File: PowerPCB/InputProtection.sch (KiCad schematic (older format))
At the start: 5 parts

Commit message: Added footprints for resistors and capacitors
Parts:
- C9: footprint (none) -> Capacitor_SMD:C_0805_2012Metric_Pad1.15x1.40mm_HandSolder
- D6, D7: footprint SOD3716X145N -> SamacSys_Parts:SOD3716X145N
- R17, R18: footprint (none) -> Resistor_SMD:R_0805_2012Metric_Pad1.15x1.40mm_HandSolder
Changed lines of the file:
@@
 $Descr A4 11693 8268
 encoding utf-8
-Sheet 4 5
+Sheet 5 5
 Title ""
 Date ""
@@
 F 0 "R21" V 1193 1850 50  0000 C CNN
 F 1 "10" V 1284 1850 50  0000 C CNN
-F 2 "" V 1330 1850 50  0001 C CNN
+F 2 "Resistor_SMD:R_0805_2012Metric_Pad1.15x1.40mm_HandSolder" V 1330 1850 50  0001 C CNN
 F 3 "~" H 1400 1850 50  0001 C CNN
 	1    1400 1850
@@
 F 0 "C11" H 2665 2296 50  0000 L CNN
 F 1 "10u" H 2665 2205 50  0000 L CNN
-F 2 "" H 2588 2100 50  0001 C CNN
+F 2 "Capacitor_SMD:C_0805_2012Metric_Pad1.15x1.40mm_HandSolder" H 2588 2100 50  0001 C CNN
 F 3 "~" H 2550 2250 50  0001 C CNN
 	1    2550 2250
@@
 F 0 "R22" V 1943 1850 50  0000 C CNN
 F 1 "1k" V 2034 1850 50  0000 C CNN
-F 2 "" V 2080 1850 50  0001 C CNN
+F 2 "Resistor_SMD:R_0805_2012Metric_Pad1.15x1.40mm_HandSolder" V 2080 1850 50  0001 C CNN
 F 3 "~" H 2150 1850 50  0001 C CNN
 	1    2150 1850
@@
 F 0 "D10" V 1904 1178 50  0000 L CNN
 F 1 "1N5819HW-7-F" V 1995 1178 50  0000 L CNN
-F 2 "SOD3716X145N" H 2100 1050 50  0001 L CNN
+F 2 "SamacSys_Parts:SOD3716X145N" H 2100 1050 50  0001 L CNN
 F 3 "http://www.diodes.com/_files/datasheets/ds30217.pdf" H 2100 950 50  0001 L CNN
 F 4 "Diode Schottky 1A 40V SOD123 Diodes Inc 1N5819HW-7-F, SMT Schottky Diode, 40V 1A, 2-Pin SOD-123" H 2100 850 50  0001 L CNN "Description"
@@
 F 0 "D11" V 1904 2078 50  0000 L CNN
 F 1 "1N5819HW-7-F" V 1995 2078 50  0000 L CNN
-F 2 "SOD3716X145N" H 2100 1950 50  0001 L CNN
+F 2 "SamacSys_Parts:SOD3716X145N" H 2100 1950 50  0001 L CNN
 F 3 "http://www.diodes.com/_files/datasheets/ds30217.pdf" H 2100 1850 50  0001 L CNN
 F 4 "Diode Schottky 1A 40V SOD123 Diodes Inc 1N5819HW-7-F, SMT Schottky Diode, 40V 1A, 2-Pin SOD-123" H 2100 1750 50  0001 L CNN "Description"

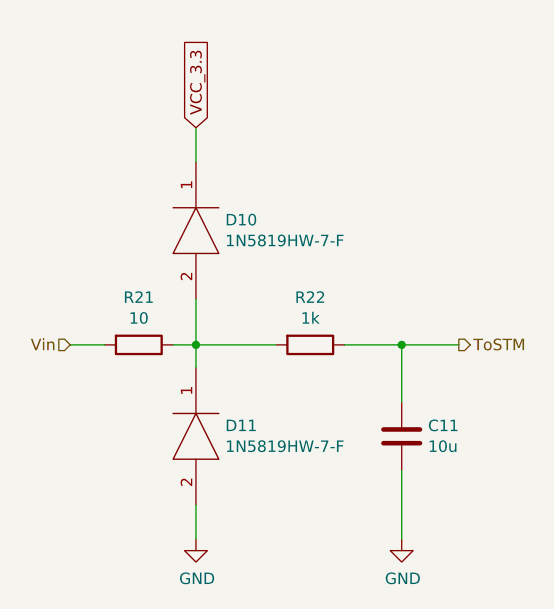
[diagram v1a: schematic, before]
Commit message: Changed Shottky diodes to 0805 size
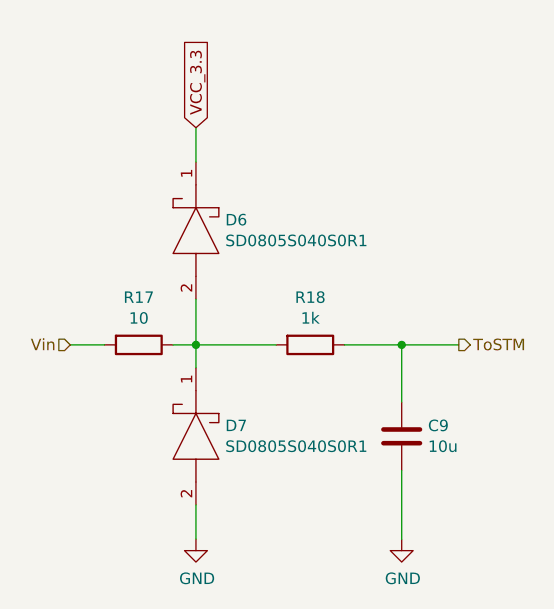
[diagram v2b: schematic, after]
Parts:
- removed D6, D7: 1N5819HW-7-F, SamacSys_Parts:SOD3716X145N, symbol SamacSys_Parts:1N5819HW-7-F
- added D8, D9: SD0805S040S0R1, SamacSys_Parts:DIOM2013X100N, symbol SamacSys_Parts:SD0805S040S0R1
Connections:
- net GND: now also D9.2
- net VCC_3.3: now also D8.1
- net at R17.1, R18.2: now also D8.2, D9.1
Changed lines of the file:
@@
 $Descr A4 11693 8268
 encoding utf-8
-Sheet 5 5
+Sheet 3 5
 Title ""
 Date ""
@@
 AR Path="/5EE3728E/5EE2BE9C" Ref="R19"  Part="1"
 AR Path="/5EE40591/5EE2BE9C" Ref="R21"  Part="1"
-F 0 "R21" V 1193 1850 50  0000 C CNN
+F 0 "R17" V 1193 1850 50  0000 C CNN
 F 1 "10" V 1284 1850 50  0000 C CNN
 F 2 "Resistor_SMD:R_0805_2012Metric_Pad1.15x1.40mm_HandSolder" V 1330 1850 50  0001 C CNN
@@
 AR Path="/5EE3728E/5EE2CD90" Ref="C10"  Part="1"
 AR Path="/5EE40591/5EE2CD90" Ref="C11"  Part="1"
-F 0 "C11" H 2665 2296 50  0000 L CNN
+F 0 "C9" H 2665 2296 50  0000 L CNN
 F 1 "10u" H 2665 2205 50  0000 L CNN
 F 2 "Capacitor_SMD:C_0805_2012Metric_Pad1.15x1.40mm_HandSolder" H 2588 2100 50  0001 C CNN
@@
 AR Path="/5EE3728E/5EE2F40D" Ref="R20"  Part="1"
 AR Path="/5EE40591/5EE2F40D" Ref="R22"  Part="1"
-F 0 "R22" V 1943 1850 50  0000 C CNN
+F 0 "R18" V 1943 1850 50  0000 C CNN
 F 1 "1k" V 2034 1850 50  0000 C CNN
 F 2 "Resistor_SMD:R_0805_2012Metric_Pad1.15x1.40mm_HandSolder" V 2080 1850 50  0001 C CNN
@@
 AR Path="/5EE3728E/5EE31FD8" Ref="#PWR025"  Part="1"
 AR Path="/5EE40591/5EE31FD8" Ref="#PWR027"  Part="1"
-F 0 "#PWR027" H 1650 2450 50  0001 C CNN
+F 0 "#PWR023" H 1650 2450 50  0001 C CNN
 F 1 "GND" H 1655 2527 50  0000 C CNN
 F 2 "" H 1650 2700 50  0001 C CNN
@@
 AR Path="/5EE3728E/5EE33069" Ref="#PWR026"  Part="1"
 AR Path="/5EE40591/5EE33069" Ref="#PWR028"  Part="1"
-F 0 "#PWR028" H 2550 2450 50  0001 C CNN
+F 0 "#PWR024" H 2550 2450 50  0001 C CNN
 F 1 "GND" H 2555 2527 50  0000 C CNN
 F 2 "" H 2550 2700 50  0001 C CNN
@@
 Text HLabel 2800 1850 2    50   Output ~ 0
 ToSTM
-$Comp
-L SamacSys_Parts:1N5819HW-7-F D6
-U 1 1 5EE2FF26
-P 1650 1050
-AR Path="/5EE2B52D/5EE2FF26" Ref="D6"  Part="1"
-AR Path="/5EE3728E/5EE2FF26" Ref="D8"  Part="1"
-AR Path="/5EE40591/5EE2FF26" Ref="D10"  Part="1"
-F 0 "D10" V 1904 1178 50  0000 L CNN
-F 1 "1N5819HW-7-F" V 1995 1178 50  0000 L CNN
-F 2 "SamacSys_Parts:SOD3716X145N" H 2100 1050 50  0001 L CNN
-F 3 "http://www.diodes.com/_files/datasheets/ds30217.pdf" H 2100 950 50  0001 L CNN
-F 4 "Diode Schottky 1A 40V SOD123 Diodes Inc 1N5819HW-7-F, SMT Schottky Diode, 40V 1A, 2-Pin SOD-123" H 2100 850 50  0001 L CNN "Description"
-F 5 "1.45" H 2100 750 50  0001 L CNN "Height"
-F 6 "621-1N5819HW-F" H 2100 650 50  0001 L CNN "Mouser Part Number"
-F 7 "https://www.mouser.co.uk/ProductDetail/Diodes-Incorporated/1N5819HW-7-F?qs=NQ47qNm99eDyWTEd07miYA%3D%3D" H 2100 550 50  0001 L CNN "Mouser Price/Stock"
-F 8 "Diodes Inc." H 2100 450 50  0001 L CNN "Manufacturer_Name"
-F 9 "1N5819HW-7-F" H 2100 350 50  0001 L CNN "Manufacturer_Part_Number"
-	1    1650 1050
-	0    1    1    0
-$EndComp
-$Comp
-L SamacSys_Parts:1N5819HW-7-F D7
-U 1 1 5EE3329F
-P 1650 1950
-AR Path="/5EE2B52D/5EE3329F" Ref="D7"  Part="1"
-AR Path="/5EE3728E/5EE3329F" Ref="D9"  Part="1"
-AR Path="/5EE40591/5EE3329F" Ref="D11"  Part="1"
-F 0 "D11" V 1904 2078 50  0000 L CNN
-F 1 "1N5819HW-7-F" V 1995 2078 50  0000 L CNN
-F 2 "SamacSys_Parts:SOD3716X145N" H 2100 1950 50  0001 L CNN
-F 3 "http://www.diodes.com/_files/datasheets/ds30217.pdf" H 2100 1850 50  0001 L CNN
-F 4 "Diode Schottky 1A 40V SOD123 Diodes Inc 1N5819HW-7-F, SMT Schottky Diode, 40V 1A, 2-Pin SOD-123" H 2100 1750 50  0001 L CNN "Description"
-F 5 "1.45" H 2100 1650 50  0001 L CNN "Height"
-F 6 "621-1N5819HW-F" H 2100 1550 50  0001 L CNN "Mouser Part Number"
-F 7 "https://www.mouser.co.uk/ProductDetail/Diodes-Incorporated/1N5819HW-7-F?qs=NQ47qNm99eDyWTEd07miYA%3D%3D" H 2100 1450 50  0001 L CNN "Mouser Price/Stock"
-F 8 "Diodes Inc." H 2100 1350 50  0001 L CNN "Manufacturer_Name"
-F 9 "1N5819HW-7-F" H 2100 1250 50  0001 L CNN "Manufacturer_Part_Number"
-	1    1650 1950
-	0    1    1    0
-$EndComp
 Wire Wire Line
 	2550 2400 2550 2700
@@
 Wire Wire Line
 	2550 1850 2800 1850
+$Comp
+L SamacSys_Parts:SD0805S040S0R1 D8
+U 1 1 5EE55C00
+P 1650 950
+AR Path="/5EE3728E/5EE55C00" Ref="D8"  Part="1"
+AR Path="/5EE2B52D/5EE55C00" Ref="D6"  Part="1"
+AR Path="/5EE40591/5EE55C00" Ref="D10"  Part="1"
+F 0 "D6" V 2004 1078 50  0000 L CNN
+F 1 "SD0805S040S0R1" V 2095 1078 50  0000 L CNN
+F 2 "SamacSys_Parts:DIOM2013X100N" H 2150 1100 50  0001 L CNN
+F 3 "https://componentsearchengine.com/Datasheets/1/SD0805S040S0R1.pdf" H 2150 1000 50  0001 L CNN
+F 4 "Schottky Diodes & Rectifiers 40volts 0.1A SIZE 0805" H 2150 900 50  0001 L CNN "Description"
+F 5 "1" H 2150 800 50  0001 L CNN "Height"
+F 6 "581-SD0805S040S0R1" H 2150 700 50  0001 L CNN "Mouser Part Number"
+F 7 "https://www.mouser.co.uk/ProductDetail/AVX/SD0805S040S0R1?qs=jCA%252BPfw4LHYgtNhiwPuw4Q%3D%3D" H 2150 600 50  0001 L CNN "Mouser Price/Stock"
+F 8 "AVX" H 2150 500 50  0001 L CNN "Manufacturer_Name"
+F 9 "SD0805S040S0R1" H 2150 400 50  0001 L CNN "Manufacturer_Part_Number"
+	1    1650 950
+	0    1    1    0
+$EndComp
+$Comp
+L SamacSys_Parts:SD0805S040S0R1 D9
+U 1 1 5EE57F4B
+P 1650 1850
+AR Path="/5EE3728E/5EE57F4B" Ref="D9"  Part="1"
+AR Path="/5EE2B52D/5EE57F4B" Ref="D7"  Part="1"
+AR Path="/5EE40591/5EE57F4B" Ref="D11"  Part="1"
+F 0 "D7" V 2004 1978 50  0000 L CNN
+F 1 "SD0805S040S0R1" V 2095 1978 50  0000 L CNN
+F 2 "SamacSys_Parts:DIOM2013X100N" H 2150 2000 50  0001 L CNN
+F 3 "https://componentsearchengine.com/Datasheets/1/SD0805S040S0R1.pdf" H 2150 1900 50  0001 L CNN
+F 4 "Schottky Diodes & Rectifiers 40volts 0.1A SIZE 0805" H 2150 1800 50  0001 L CNN "Description"
+F 5 "1" H 2150 1700 50  0001 L CNN "Height"
+F 6 "581-SD0805S040S0R1" H 2150 1600 50  0001 L CNN "Mouser Part Number"
+F 7 "https://www.mouser.co.uk/ProductDetail/AVX/SD0805S040S0R1?qs=jCA%252BPfw4LHYgtNhiwPuw4Q%3D%3D" H 2150 1500 50  0001 L CNN "Mouser Price/Stock"
+F 8 "AVX" H 2150 1400 50  0001 L CNN "Manufacturer_Name"
+F 9 "SD0805S040S0R1" H 2150 1300 50  0001 L CNN "Manufacturer_Part_Number"
+	1    1650 1850
+	0    1    1    0
+$EndComp
 $EndSCHEMATC

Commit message: Added bypass capacitors to CAN transceivers
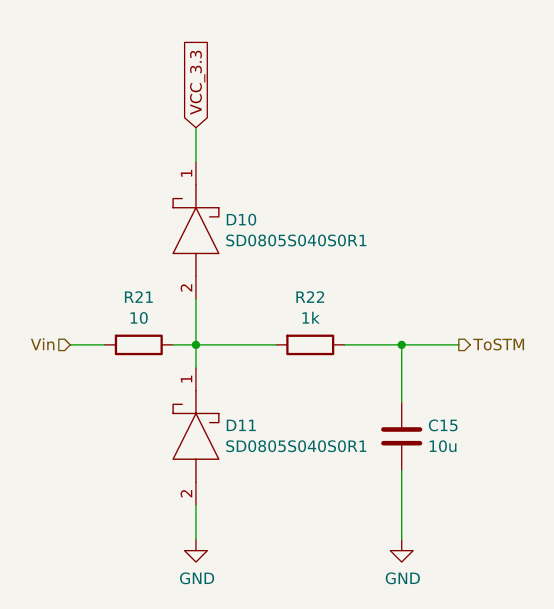
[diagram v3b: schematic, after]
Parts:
- renumbered C9 to C13
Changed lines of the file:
@@
 AR Path="/5EE3728E/5EE2BE9C" Ref="R19"  Part="1"
 AR Path="/5EE40591/5EE2BE9C" Ref="R21"  Part="1"
-F 0 "R17" V 1193 1850 50  0000 C CNN
+F 0 "R21" V 1193 1850 50  0000 C CNN
 F 1 "10" V 1284 1850 50  0000 C CNN
 F 2 "Resistor_SMD:R_0805_2012Metric_Pad1.15x1.40mm_HandSolder" V 1330 1850 50  0001 C CNN
@@
 $EndComp
 $Comp
-L Device:C C9
+L Device:C C13
 U 1 1 5EE2CD90
 P 2550 2250
-AR Path="/5EE2B52D/5EE2CD90" Ref="C9"  Part="1"
-AR Path="/5EE3728E/5EE2CD90" Ref="C10"  Part="1"
-AR Path="/5EE40591/5EE2CD90" Ref="C11"  Part="1"
-F 0 "C9" H 2665 2296 50  0000 L CNN
+AR Path="/5EE2B52D/5EE2CD90" Ref="C13"  Part="1"
+AR Path="/5EE3728E/5EE2CD90" Ref="C14"  Part="1"
+AR Path="/5EE40591/5EE2CD90" Ref="C15"  Part="1"
+F 0 "C15" H 2665 2296 50  0000 L CNN
 F 1 "10u" H 2665 2205 50  0000 L CNN
 F 2 "Capacitor_SMD:C_0805_2012Metric_Pad1.15x1.40mm_HandSolder" H 2588 2100 50  0001 C CNN
@@
 AR Path="/5EE3728E/5EE2F40D" Ref="R20"  Part="1"
 AR Path="/5EE40591/5EE2F40D" Ref="R22"  Part="1"
-F 0 "R18" V 1943 1850 50  0000 C CNN
+F 0 "R22" V 1943 1850 50  0000 C CNN
 F 1 "1k" V 2034 1850 50  0000 C CNN
 F 2 "Resistor_SMD:R_0805_2012Metric_Pad1.15x1.40mm_HandSolder" V 2080 1850 50  0001 C CNN
@@
 	1650 1950 1650 1850
 $Comp
-L power:GND #PWR023
+L power:GND #PWR028
 U 1 1 5EE31FD8
 P 1650 2700
-AR Path="/5EE2B52D/5EE31FD8" Ref="#PWR023"  Part="1"
-AR Path="/5EE3728E/5EE31FD8" Ref="#PWR025"  Part="1"
-AR Path="/5EE40591/5EE31FD8" Ref="#PWR027"  Part="1"
-F 0 "#PWR023" H 1650 2450 50  0001 C CNN
+AR Path="/5EE2B52D/5EE31FD8" Ref="#PWR028"  Part="1"
+AR Path="/5EE3728E/5EE31FD8" Ref="#PWR030"  Part="1"
+AR Path="/5EE40591/5EE31FD8" Ref="#PWR032"  Part="1"
+F 0 "#PWR032" H 1650 2450 50  0001 C CNN
 F 1 "GND" H 1655 2527 50  0000 C CNN
 F 2 "" H 1650 2700 50  0001 C CNN
@@
 	1650 2700 1650 2550
 $Comp
-L power:GND #PWR024
+L power:GND #PWR029
 U 1 1 5EE33069
 P 2550 2700
-AR Path="/5EE2B52D/5EE33069" Ref="#PWR024"  Part="1"
-AR Path="/5EE3728E/5EE33069" Ref="#PWR026"  Part="1"
-AR Path="/5EE40591/5EE33069" Ref="#PWR028"  Part="1"
-F 0 "#PWR024" H 2550 2450 50  0001 C CNN
+AR Path="/5EE2B52D/5EE33069" Ref="#PWR029"  Part="1"
+AR Path="/5EE3728E/5EE33069" Ref="#PWR031"  Part="1"
+AR Path="/5EE40591/5EE33069" Ref="#PWR033"  Part="1"
+F 0 "#PWR033" H 2550 2450 50  0001 C CNN
 F 1 "GND" H 2555 2527 50  0000 C CNN
 F 2 "" H 2550 2700 50  0001 C CNN
@@
 	2550 1850 2800 1850
 $Comp
+L SamacSys_Parts:SD0805S040S0R1 D9
+U 1 1 5EE57F4B
+P 1650 1850
+AR Path="/5EE3728E/5EE57F4B" Ref="D9"  Part="1"
+AR Path="/5EE2B52D/5EE57F4B" Ref="D7"  Part="1"
+AR Path="/5EE40591/5EE57F4B" Ref="D11"  Part="1"
+F 0 "D11" V 2004 1978 50  0000 L CNN
+F 1 "SD0805S040S0R1" V 2095 1978 50  0000 L CNN
+F 2 "SamacSys_Parts:DIOM2013X100N" H 2150 2000 50  0001 L CNN
+F 3 "https://componentsearchengine.com/Datasheets/1/SD0805S040S0R1.pdf" H 2150 1900 50  0001 L CNN
+F 4 "Schottky Diodes & Rectifiers 40volts 0.1A SIZE 0805" H 2150 1800 50  0001 L CNN "Description"
+F 5 "1" H 2150 1700 50  0001 L CNN "Height"
+F 6 "581-SD0805S040S0R1" H 2150 1600 50  0001 L CNN "Mouser Part Number"
+F 7 "https://www.mouser.co.uk/ProductDetail/AVX/SD0805S040S0R1?qs=jCA%252BPfw4LHYgtNhiwPuw4Q%3D%3D" H 2150 1500 50  0001 L CNN "Mouser Price/Stock"
+F 8 "AVX" H 2150 1400 50  0001 L CNN "Manufacturer_Name"
+F 9 "SD0805S040S0R1" H 2150 1300 50  0001 L CNN "Manufacturer_Part_Number"
+	1    1650 1850
+	0    1    1    0
+$EndComp
+$Comp
 L SamacSys_Parts:SD0805S040S0R1 D8
 U 1 1 5EE55C00
@@
 AR Path="/5EE2B52D/5EE55C00" Ref="D6"  Part="1"
 AR Path="/5EE40591/5EE55C00" Ref="D10"  Part="1"
-F 0 "D6" V 2004 1078 50  0000 L CNN
+F 0 "D10" V 2004 1078 50  0000 L CNN
 F 1 "SD0805S040S0R1" V 2095 1078 50  0000 L CNN
 F 2 "SamacSys_Parts:DIOM2013X100N" H 2150 1100 50  0001 L CNN
@@
 	0    1    1    0
 $EndComp
-$Comp
-L SamacSys_Parts:SD0805S040S0R1 D9
-U 1 1 5EE57F4B
-P 1650 1850
-AR Path="/5EE3728E/5EE57F4B" Ref="D9"  Part="1"
-AR Path="/5EE2B52D/5EE57F4B" Ref="D7"  Part="1"
-AR Path="/5EE40591/5EE57F4B" Ref="D11"  Part="1"
-F 0 "D7" V 2004 1978 50  0000 L CNN
-F 1 "SD0805S040S0R1" V 2095 1978 50  0000 L CNN
-F 2 "SamacSys_Parts:DIOM2013X100N" H 2150 2000 50  0001 L CNN
-F 3 "https://componentsearchengine.com/Datasheets/1/SD0805S040S0R1.pdf" H 2150 1900 50  0001 L CNN
-F 4 "Schottky Diodes & Rectifiers 40volts 0.1A SIZE 0805" H 2150 1800 50  0001 L CNN "Description"
-F 5 "1" H 2150 1700 50  0001 L CNN "Height"
-F 6 "581-SD0805S040S0R1" H 2150 1600 50  0001 L CNN "Mouser Part Number"
-F 7 "https://www.mouser.co.uk/ProductDetail/AVX/SD0805S040S0R1?qs=jCA%252BPfw4LHYgtNhiwPuw4Q%3D%3D" H 2150 1500 50  0001 L CNN "Mouser Price/Stock"
-F 8 "AVX" H 2150 1400 50  0001 L CNN "Manufacturer_Name"
-F 9 "SD0805S040S0R1" H 2150 1300 50  0001 L CNN "Manufacturer_Part_Number"
-	1    1650 1850
-	0    1    1    0
-$EndComp

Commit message: Added VDD bypass capacitors and values for all components
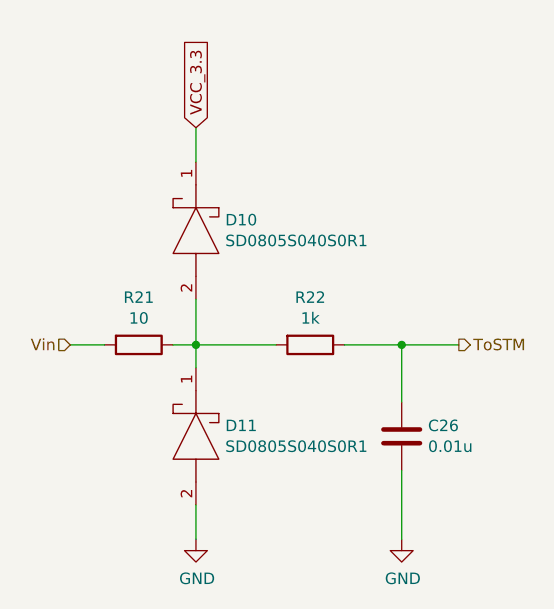
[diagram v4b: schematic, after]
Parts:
- C24: renamed from C13; value 10u -> 0.01u
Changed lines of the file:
@@
 $Descr A4 11693 8268
 encoding utf-8
-Sheet 3 5
+Sheet 5 5
 Title ""
 Date ""
@@
 $EndComp
 $Comp
-L Device:C C13
+L Device:C C24
 U 1 1 5EE2CD90
 P 2550 2250
-AR Path="/5EE2B52D/5EE2CD90" Ref="C13"  Part="1"
-AR Path="/5EE3728E/5EE2CD90" Ref="C14"  Part="1"
-AR Path="/5EE40591/5EE2CD90" Ref="C15"  Part="1"
-F 0 "C15" H 2665 2296 50  0000 L CNN
-F 1 "10u" H 2665 2205 50  0000 L CNN
+AR Path="/5EE2B52D/5EE2CD90" Ref="C24"  Part="1"
+AR Path="/5EE3728E/5EE2CD90" Ref="C25"  Part="1"
+AR Path="/5EE40591/5EE2CD90" Ref="C26"  Part="1"
+F 0 "C26" H 2665 2296 50  0000 L CNN
+F 1 "0.01u" H 2665 2205 50  0000 L CNN
 F 2 "Capacitor_SMD:C_0805_2012Metric_Pad1.15x1.40mm_HandSolder" H 2588 2100 50  0001 C CNN
 F 3 "~" H 2550 2250 50  0001 C CNN
@@
 	1650 1950 1650 1850
 $Comp
-L power:GND #PWR028
+L power:GND #PWR039
 U 1 1 5EE31FD8
 P 1650 2700
-AR Path="/5EE2B52D/5EE31FD8" Ref="#PWR028"  Part="1"
-AR Path="/5EE3728E/5EE31FD8" Ref="#PWR030"  Part="1"
-AR Path="/5EE40591/5EE31FD8" Ref="#PWR032"  Part="1"
-F 0 "#PWR032" H 1650 2450 50  0001 C CNN
+AR Path="/5EE2B52D/5EE31FD8" Ref="#PWR039"  Part="1"
+AR Path="/5EE3728E/5EE31FD8" Ref="#PWR041"  Part="1"
+AR Path="/5EE40591/5EE31FD8" Ref="#PWR043"  Part="1"
+F 0 "#PWR043" H 1650 2450 50  0001 C CNN
 F 1 "GND" H 1655 2527 50  0000 C CNN
 F 2 "" H 1650 2700 50  0001 C CNN
@@
 	1650 2700 1650 2550
 $Comp
-L power:GND #PWR029
+L power:GND #PWR040
 U 1 1 5EE33069
 P 2550 2700
-AR Path="/5EE2B52D/5EE33069" Ref="#PWR029"  Part="1"
-AR Path="/5EE3728E/5EE33069" Ref="#PWR031"  Part="1"
-AR Path="/5EE40591/5EE33069" Ref="#PWR033"  Part="1"
-F 0 "#PWR033" H 2550 2450 50  0001 C CNN
+AR Path="/5EE2B52D/5EE33069" Ref="#PWR040"  Part="1"
+AR Path="/5EE3728E/5EE33069" Ref="#PWR042"  Part="1"
+AR Path="/5EE40591/5EE33069" Ref="#PWR044"  Part="1"
+F 0 "#PWR044" H 2550 2450 50  0001 C CNN
 F 1 "GND" H 2555 2527 50  0000 C CNN
 F 2 "" H 2550 2700 50  0001 C CNN

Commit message: Added pull-down resistors to usused pins
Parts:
- renumbered C24 to C26, R17 to R21, R18 to R22
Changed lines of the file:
@@
 $Descr A4 11693 8268
 encoding utf-8
-Sheet 5 5
+Sheet 3 109
 Title ""
 Date ""
@@
 $EndDescr
 $Comp
-L Device:R R17
+L Device:R R21
 U 1 1 5EE2BE9C
 P 1400 1850
-AR Path="/5EE2B52D/5EE2BE9C" Ref="R17"  Part="1"
+AR Path="/5EE2B52D/5EE2BE9C" Ref="R21"  Part="1"
 AR Path="/5EE3728E/5EE2BE9C" Ref="R19"  Part="1"
-AR Path="/5EE40591/5EE2BE9C" Ref="R21"  Part="1"
+AR Path="/5EE40591/5EE2BE9C" Ref="R17"  Part="1"
 F 0 "R21" V 1193 1850 50  0000 C CNN
 F 1 "10" V 1284 1850 50  0000 C CNN
@@
 $EndComp
 $Comp
-L Device:C C24
+L Device:C C26
 U 1 1 5EE2CD90
 P 2550 2250
-AR Path="/5EE2B52D/5EE2CD90" Ref="C24"  Part="1"
+AR Path="/5EE2B52D/5EE2CD90" Ref="C26"  Part="1"
 AR Path="/5EE3728E/5EE2CD90" Ref="C25"  Part="1"
-AR Path="/5EE40591/5EE2CD90" Ref="C26"  Part="1"
+AR Path="/5EE40591/5EE2CD90" Ref="C24"  Part="1"
 F 0 "C26" H 2665 2296 50  0000 L CNN
 F 1 "0.01u" H 2665 2205 50  0000 L CNN
@@
 	1650 1850 1550 1850
 $Comp
-L Device:R R18
+L Device:R R22
 U 1 1 5EE2F40D
 P 2150 1850
-AR Path="/5EE2B52D/5EE2F40D" Ref="R18"  Part="1"
+AR Path="/5EE2B52D/5EE2F40D" Ref="R22"  Part="1"
 AR Path="/5EE3728E/5EE2F40D" Ref="R20"  Part="1"
-AR Path="/5EE40591/5EE2F40D" Ref="R22"  Part="1"
+AR Path="/5EE40591/5EE2F40D" Ref="R18"  Part="1"
 F 0 "R22" V 1943 1850 50  0000 C CNN
 F 1 "1k" V 2034 1850 50  0000 C CNN
@@
 	1650 1950 1650 1850
 $Comp
-L power:GND #PWR039
+L power:GND #PWR043
 U 1 1 5EE31FD8
 P 1650 2700
-AR Path="/5EE2B52D/5EE31FD8" Ref="#PWR039"  Part="1"
+AR Path="/5EE2B52D/5EE31FD8" Ref="#PWR043"  Part="1"
 AR Path="/5EE3728E/5EE31FD8" Ref="#PWR041"  Part="1"
-AR Path="/5EE40591/5EE31FD8" Ref="#PWR043"  Part="1"
+AR Path="/5EE40591/5EE31FD8" Ref="#PWR039"  Part="1"
 F 0 "#PWR043" H 1650 2450 50  0001 C CNN
 F 1 "GND" H 1655 2527 50  0000 C CNN
@@
 	1650 2700 1650 2550
 $Comp
-L power:GND #PWR040
+L power:GND #PWR044
 U 1 1 5EE33069
 P 2550 2700
-AR Path="/5EE2B52D/5EE33069" Ref="#PWR040"  Part="1"
+AR Path="/5EE2B52D/5EE33069" Ref="#PWR044"  Part="1"
 AR Path="/5EE3728E/5EE33069" Ref="#PWR042"  Part="1"
-AR Path="/5EE40591/5EE33069" Ref="#PWR044"  Part="1"
+AR Path="/5EE40591/5EE33069" Ref="#PWR040"  Part="1"
 F 0 "#PWR044" H 2550 2450 50  0001 C CNN
 F 1 "GND" H 2555 2527 50  0000 C CNN
@@
 P 1650 1850
 AR Path="/5EE3728E/5EE57F4B" Ref="D9"  Part="1"
-AR Path="/5EE2B52D/5EE57F4B" Ref="D7"  Part="1"
-AR Path="/5EE40591/5EE57F4B" Ref="D11"  Part="1"
+AR Path="/5EE2B52D/5EE57F4B" Ref="D11"  Part="1"
+AR Path="/5EE40591/5EE57F4B" Ref="D7"  Part="1"
 F 0 "D11" V 2004 1978 50  0000 L CNN
 F 1 "SD0805S040S0R1" V 2095 1978 50  0000 L CNN
@@
 P 1650 950
 AR Path="/5EE3728E/5EE55C00" Ref="D8"  Part="1"
-AR Path="/5EE2B52D/5EE55C00" Ref="D6"  Part="1"
-AR Path="/5EE40591/5EE55C00" Ref="D10"  Part="1"
+AR Path="/5EE2B52D/5EE55C00" Ref="D10"  Part="1"
+AR Path="/5EE40591/5EE55C00" Ref="D6"  Part="1"
 F 0 "D10" V 2004 1078 50  0000 L CNN
 F 1 "SD0805S040S0R1" V 2095 1078 50  0000 L CNN
